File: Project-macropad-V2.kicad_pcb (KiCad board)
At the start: 2 copper layers, 50 parts, among them J1 Conn_01x04_Male, SW1 RotaryEncoder_Switch, SW2 SW_Push, SW3 SW_SPDT

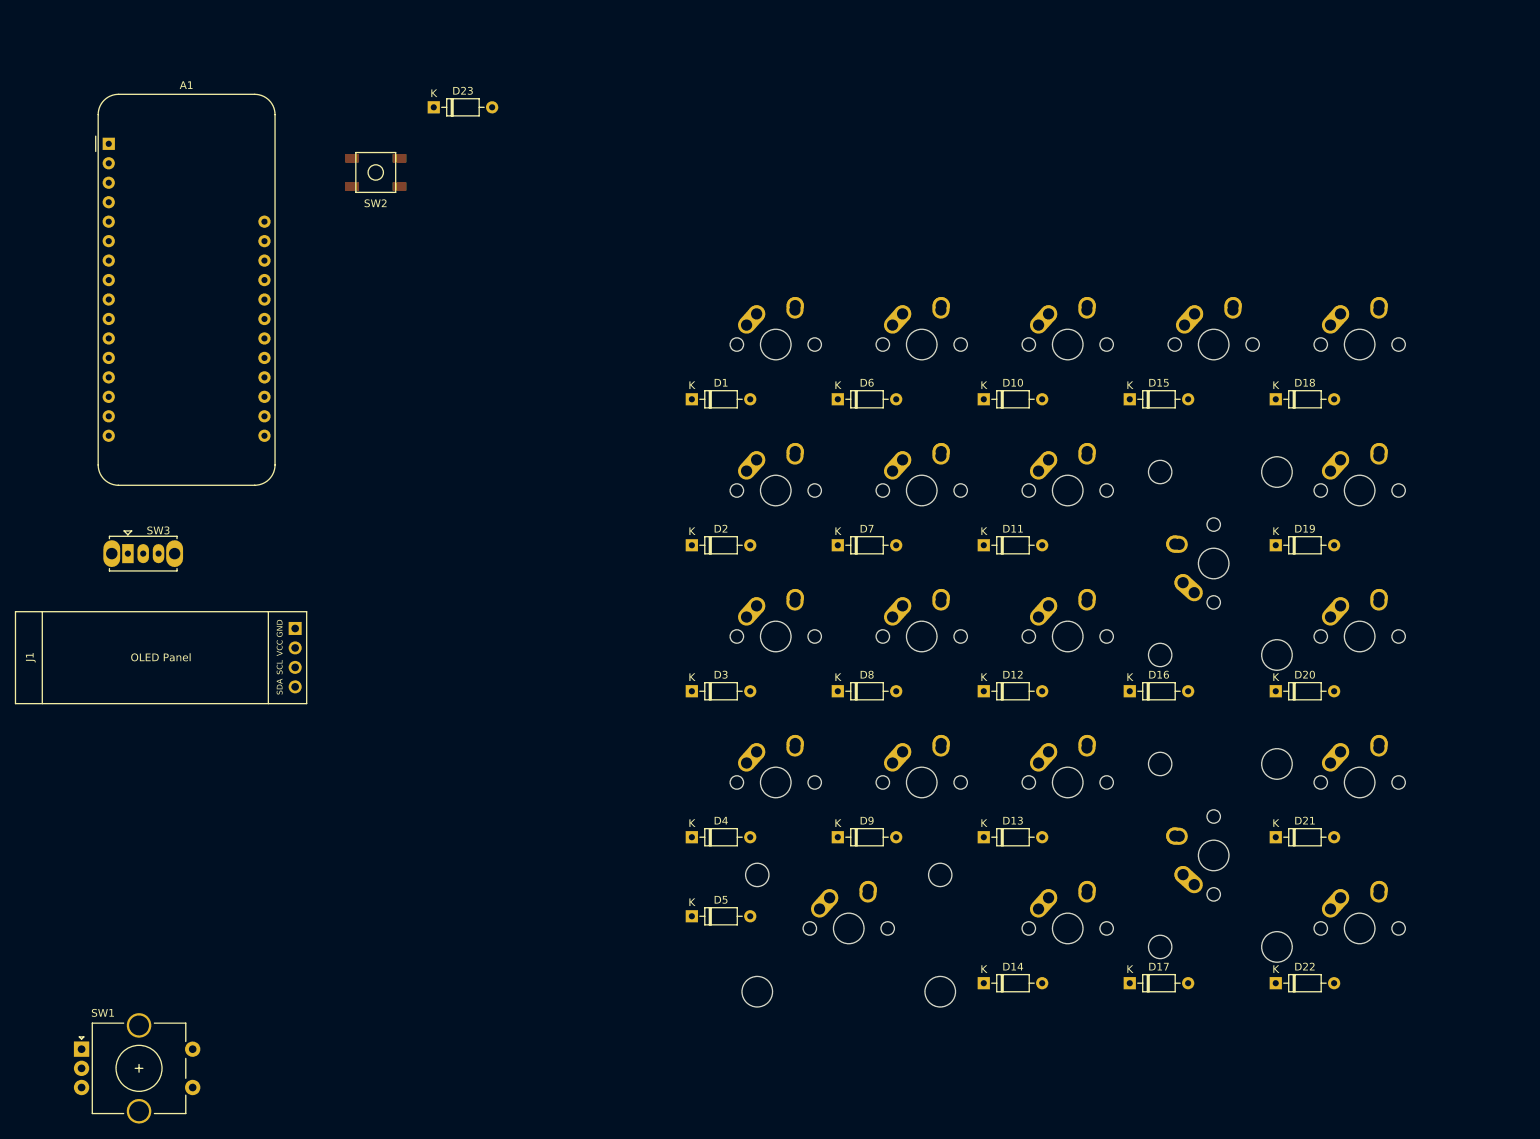
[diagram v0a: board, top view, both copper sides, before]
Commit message: PCB Routing done
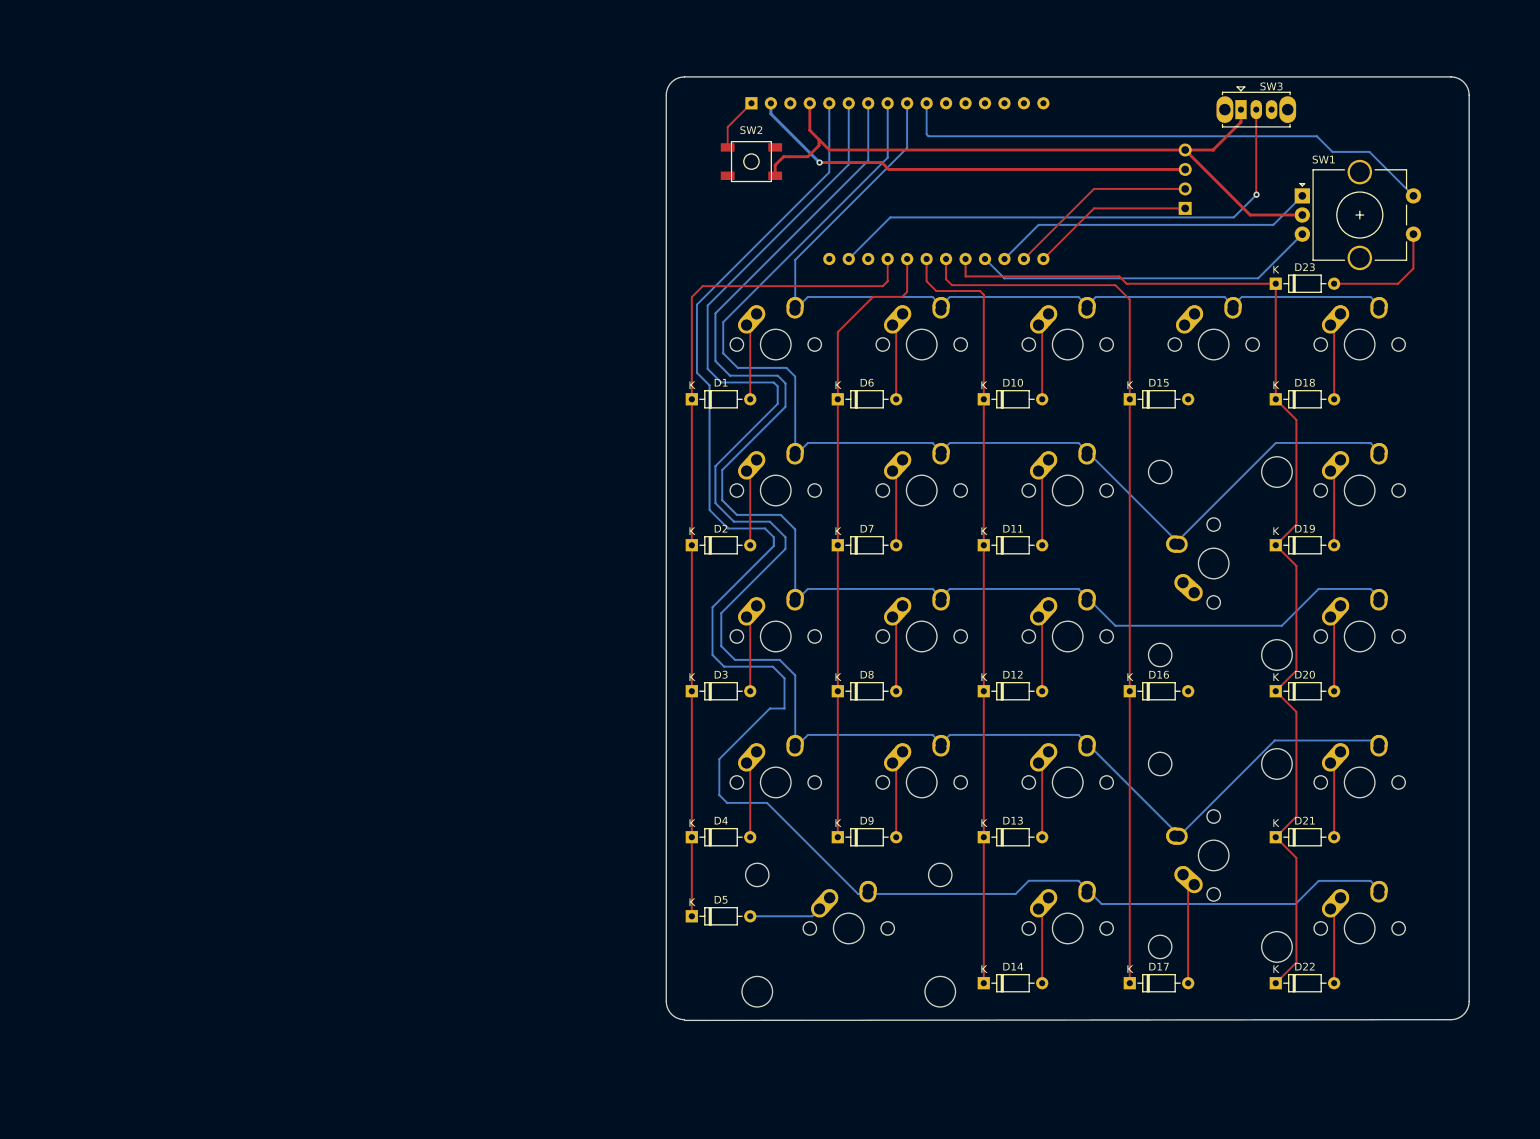
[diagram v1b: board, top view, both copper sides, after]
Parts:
- A1, J1: moved to B.Cu
- moved SW1 194.4 mm to (189.4, 37.7)
- moved SW3 156.4 mm to (181.4, 26.5)
- moved J1 126.6 mm to (137.6, 41.6)
- moved D23 112.3 mm to (185.9, 49.2)
- moved A1 84.0 mm to (117.5, 25.7), turned to -90 degrees
- moved SW2 49.0 mm to (117.5, 33.3), turned to 180 degrees
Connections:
- A1 pad 10: ROT2 -> ROW0
- A1 pad 19: ROW0 -> ROT1
- A1 pad 20: ROW1 -> ROT2
- A1 pad 21: ROW2 -> COL4
- A1 pad 22: ROW3 -> COL3
- A1 pad 23: ROW4 -> COL2
- A1 pad 24: ROW5 -> COL1
- A1 pad 25: ROT1 -> COL0
- A1 pad 5: COL0 -> ROW5
- A1 pad 6: COL1 -> ROW4
- A1 pad 7: COL2 -> ROW3
- A1 pad 8: COL3 -> ROW2
- A1 pad 9: COL4 -> ROW1
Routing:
- net ROW5: track 0.00 -> 215.1 mm
- net ROW4: track 0.00 -> 208.8 mm
- net ROW3: track 0.00 -> 173.8 mm
- net ROW2: track 0.00 -> 151.6 mm
- net COL4: track 0.00 -> 143.4 mm
- net COL3: track 0.00 -> 116.9 mm
- net ROW1: track 0.00 -> 112.7 mm
- net COL0: track 0.00 -> 110.1 mm
- net COL2: track 0.00 -> 100.9 mm
- net GND: track 0.00 -> 92.6 mm
- net COL1: track 0.00 -> 81.4 mm
- net ROW0: track 0.00 -> 70.9 mm
- net Net-(A1-Pad27): track 0.00 -> 67.8 mm, vias 0 -> 1
- net +3V3: track 0.00 -> 58.5 mm, vias 0 -> 1
- net ROT2: track 0.00 -> 44.8 mm
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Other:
- board outline added: 104.8 x 123.1 mm

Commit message: Finished PCB
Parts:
- added G***: LOGO, Dick:Dick_small, F.Cu at (205.6, 29.4)
- D1, D10, D11, D12, D13, D14, D15, D16, D17, D18, D19, D2, D20, D21, D22, D23, D3, D4, D5, D6, D7, D8, D9: moved to B.Cu
- J1: moved to F.Cu
- moved J1 12.2 mm to (137.6, 29.4)
- moved D20 5.32 mm to (190.7, 104.8)
- moved D21 5.32 mm to (190.7, 123.8)
- moved D19 5.32 mm to (190.7, 85.7)
- moved D13 3.37 mm to (150.2, 123.8)
- moved D18 3.37 mm to (188.3, 66.7)
- moved D12 2.38 mm to (147.8, 104.8)
- moved D16 2.38 mm to (166.8, 104.8)
- moved D3 2.38 mm to (109.7, 104.8)
- moved D8 2.38 mm to (128.7, 104.8)
- moved D9 2.38 mm to (128.7, 123.8)
- moved D1 2.38 mm to (109.7, 66.7)
- moved D10 2.38 mm to (147.8, 66.7)
- moved D11 2.38 mm to (147.8, 85.7)
- moved D14 2.38 mm to (147.8, 142.9)
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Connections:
- J1 pad 1: SDA -> GND
- J1 pad 2: SCL -> +3V3
- J1 pad 3: +3V3 -> SCL
- J1 pad 4: GND -> SDA
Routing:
- net Net-(D16-Pad2): track 0.00 -> 15.6 mm
- net Net-(D15-Pad2): track 0.00 -> 12.3 mm
- net Net-(D5-Pad2): track 9.44 -> 20.2 mm
- net Net-(D21-Pad2): track 9.88 -> 15.6 mm
- net Net-(D20-Pad2): track 9.88 -> 15.6 mm
- net Net-(D19-Pad2): track 9.88 -> 15.6 mm
- net COL2: track 100.9 -> 105.3 mm
- net COL4: track 143.4 -> 147.7 mm
- net Net-(D13-Pad2): track 9.88 -> 13.2 mm
- net Net-(D18-Pad2): track 9.88 -> 13.2 mm
- net Net-(D9-Pad2): track 9.88 -> 12.3 mm
- net Net-(D8-Pad2): track 9.88 -> 12.3 mm
- net Net-(D3-Pad2): track 9.88 -> 12.3 mm
- net Net-(D12-Pad2): track 9.88 -> 12.3 mm
- net COL1: track 81.4 -> 83.8 mm
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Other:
- board size 104.8 x 123.1 mm -> 104.8 x 123 mm
- board text added: "Dr.Kreijger"

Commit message: Plate almost done
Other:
- board size 104.8 x 123 mm -> 110.5 x 128.4 mm

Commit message: Plate done
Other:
- board size 110.5 x 128.4 mm -> 119.1 x 138.9 mm
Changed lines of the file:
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@@
   (gr_line (start 113.635 50.673) (end 113.635 63.673) (layer "Edge.Cuts") (width 0.2))
   (gr_line (start 203.835 88.773) (end 203.835 101.773) (layer "Edge.Cuts") (width 0.2))
-  (gr_line (start 106.26725 147.898) (end 211.219002 147.898) (layer "Edge.Cuts") (width 0.2))
-  (gr_circle (center 105.918 21.082) (end 107.518 21.082) (layer "Edge.Cuts") (width 0.2) (fill none))
+  (gr_circle (center 104.775 19.84375) (end 106.375 19.84375) (layer "Edge.Cuts") (width 0.2) (fill none))
   (gr_arc (start 189.835 126.873) (mid 189.981447 126.519447) (end 190.335 126.373) (layer "Edge.Cuts") (width 0.2))
   (gr_arc (start 152.235 83.223) (mid 151.881447 83.076553) (end 151.735 82.723) (layer "Edge.Cuts") (width 0.2))
@@
   (gr_arc (start 127.135 88.273) (mid 127.488553 88.419447) (end 127.635 88.773) (layer "Edge.Cuts") (width 0.2))
   (gr_line (start 132.685 69.723) (end 132.685 82.723) (layer "Edge.Cuts") (width 0.2))
+  (gr_arc (start 211.93125 14.2875) (mid 216.421378 16.147372) (end 218.28125 20.6375) (layer "Edge.Cuts") (width 0.2))
   (gr_line (start 132.685 50.673) (end 132.685 63.673) (layer "Edge.Cuts") (width 0.2))
   (gr_line (start 132.685 107.823) (end 132.685 120.823) (layer "Edge.Cuts") (width 0.2))
   (gr_arc (start 170.785 79.248) (mid 170.931447 78.894447) (end 171.285 78.748) (layer "Edge.Cuts") (width 0.2))
+  (gr_line (start 99.21875 20.6375) (end 99.21875 146.84375) (layer "Edge.Cuts") (width 0.2))
   (gr_arc (start 113.635 107.823) (mid 113.781447 107.469447) (end 114.135 107.323) (layer "Edge.Cuts") (width 0.2))
   (gr_line (start 113.6396 29.448) (end 113.6396 37.084) (layer "Edge.Cuts") (width 0.2))
@@
   (gr_arc (start 127.635 63.673) (mid 127.488553 64.026553) (end 127.135 64.173) (layer "Edge.Cuts") (width 0.2))
   (gr_arc (start 123.16 126.873) (mid 123.306447 126.519447) (end 123.66 126.373) (layer "Edge.Cuts") (width 0.2))
-  (gr_circle (center 212.7506 21.082) (end 214.3506 21.082) (layer "Edge.Cuts") (width 0.2) (fill none))
+  (gr_circle (center 212.725 19.84375) (end 214.325 19.84375) (layer "Edge.Cuts") (width 0.2) (fill none))
   (gr_line (start 152.235 121.323) (end 165.235 121.323) (layer "Edge.Cuts") (width 0.2))
   (gr_arc (start 203.335 50.173) (mid 203.688553 50.319447) (end 203.835 50.673) (layer "Edge.Cuts") (width 0.2))
@@
   (gr_arc (start 127.135 50.173) (mid 127.488553 50.319447) (end 127.635 50.673) (layer "Edge.Cuts") (width 0.2))
   (gr_line (start 114.135 107.323) (end 127.135 107.323) (layer "Edge.Cuts") (width 0.2))
-  (gr_line (start 213.600252 145.51675) (end 213.600252 22.09165) (layer "Edge.Cuts") (width 0.2))
-  (gr_arc (start 213.600252 145.51675) (mid 212.9028 147.200548) (end 211.219002 147.898) (layer "Edge.Cuts") (width 0.2))
   (gr_line (start 170.785 79.248) (end 170.785 92.248) (layer "Edge.Cuts") (width 0.2))
   (gr_arc (start 189.835 50.673) (mid 189.981447 50.319447) (end 190.335 50.173) (layer "Edge.Cuts") (width 0.2))
@@
   (gr_line (start 170.785 50.673) (end 170.785 63.673) (layer "Edge.Cuts") (width 0.2))
   (gr_arc (start 183.285 108.41) (mid 183.638553 108.556447) (end 183.785 108.91) (layer "Edge.Cuts") (width 0.2))
-  (gr_line (start 211.219002 19.7104) (end 106.26725 19.7104) (layer "Edge.Cuts") (width 0.2))
   (gr_line (start 190.335 88.273) (end 203.335 88.273) (layer "Edge.Cuts") (width 0.2))
   (gr_line (start 151.735 50.673) (end 151.735 63.673) (layer "Edge.Cuts") (width 0.2))
@@
   (gr_arc (start 168.785 70.81) (mid 168.931447 70.456447) (end 169.285 70.31) (layer "Edge.Cuts") (width 0.2))
   (gr_arc (start 203.835 101.773) (mid 203.688553 102.126553) (end 203.335 102.273) (layer "Edge.Cuts") (width 0.2))
+  (gr_line (start 218.28125 146.84375) (end 218.28125 20.6375) (layer "Edge.Cuts") (width 0.2))
   (gr_line (start 190.335 50.173) (end 203.335 50.173) (layer "Edge.Cuts") (width 0.2))
   (gr_arc (start 165.235 88.273) (mid 165.588553 88.419447) (end 165.735 88.773) (layer "Edge.Cuts") (width 0.2))
@@
   (gr_line (start 208.75625 22.225) (end 108.74375 22.225) (layer "Edge.Cuts") (width 0.1))
   (gr_line (start 146.685 88.773) (end 146.685 101.773) (layer "Edge.Cuts") (width 0.2))
+  (gr_arc (start 105.56875 153.19375) (mid 101.078622 151.333878) (end 99.21875 146.84375) (layer "Edge.Cuts") (width 0.2))
   (gr_arc (start 203.335 69.223) (mid 203.688553 69.369447) (end 203.835 69.723) (layer "Edge.Cuts") (width 0.2))
   (gr_arc (start 208.75625 22.225) (mid 210.440048 22.922452) (end 211.1375 24.60625) (layer "Edge.Cuts") (width 0.1))
@@
   (gr_line (start 113.635 69.723) (end 113.635 82.723) (layer "Edge.Cuts") (width 0.2))
   (gr_arc (start 189.835 88.773) (mid 189.981447 88.419447) (end 190.335 88.273) (layer "Edge.Cuts") (width 0.2))
-  (gr_arc (start 211.219002 19.7104) (mid 212.9028 20.407852) (end 213.600252 22.09165) (layer "Edge.Cuts") (width 0.2))
   (gr_line (start 189.835 69.723) (end 189.835 82.723) (layer "Edge.Cuts") (width 0.2))
   (gr_arc (start 211.1375 142.875) (mid 210.440048 144.558798) (end 208.75625 145.25625) (layer "Edge.Cuts") (width 0.1))
   (gr_line (start 183.285 115.41) (end 169.285 115.41) (layer "Edge.Cuts") (width 0.2))
+  (gr_line (start 211.93125 14.2875) (end 105.56875 14.2875) (layer "Edge.Cuts") (width 0.2))
   (gr_line (start 114.135 50.173) (end 127.135 50.173) (layer "Edge.Cuts") (width 0.2))
+  (gr_arc (start 218.28125 146.84375) (mid 216.421378 151.333878) (end 211.93125 153.19375) (layer "Edge.Cuts") (width 0.2))
   (gr_line (start 152.235 64.173) (end 165.235 64.173) (layer "Edge.Cuts") (width 0.2))
   (gr_line (start 114.135 88.273) (end 127.135 88.273) (layer "Edge.Cuts") (width 0.2))
@@
   (gr_arc (start 113.635 69.723) (mid 113.781447 69.369447) (end 114.135 69.223) (layer "Edge.Cuts") (width 0.2))
   (gr_arc (start 146.685 63.673) (mid 146.538553 64.026553) (end 146.185 64.173) (layer "Edge.Cuts") (width 0.2))
-  (gr_line (start 103.886 145.51675) (end 103.886 22.09165) (layer "Edge.Cuts") (width 0.2))
   (gr_arc (start 190.335 140.373) (mid 189.981447 140.226553) (end 189.835 139.873) (layer "Edge.Cuts") (width 0.2))
   (gr_line (start 123.66 140.373) (end 136.66 140.373) (layer "Edge.Cuts") (width 0.2))
-  (gr_arc (start 103.886 22.09165) (mid 104.583452 20.407852) (end 106.26725 19.7104) (layer "Edge.Cuts") (width 0.2))
   (gr_arc (start 146.685 101.773) (mid 146.538553 102.126553) (end 146.185 102.273) (layer "Edge.Cuts") (width 0.2))
   (gr_arc (start 113.635 88.773) (mid 113.781447 88.419447) (end 114.135 88.273) (layer "Edge.Cuts") (width 0.2))
@@
   (gr_line (start 127.635 107.823) (end 127.635 120.823) (layer "Edge.Cuts") (width 0.2))
   (gr_line (start 168.785 94.686) (end 168.785 100.686) (layer "Edge.Cuts") (width 0.2))
-  (gr_circle (center 105.918 146.1262) (end 107.518 146.1262) (layer "Edge.Cuts") (width 0.2) (fill none))
+  (gr_circle (center 104.775 147.6375) (end 106.375 147.6375) (layer "Edge.Cuts") (width 0.2) (fill none))
   (gr_line (start 108.74375 145.25625) (end 208.75625 145.25625) (layer "Edge.Cuts") (width 0.1))
   (gr_arc (start 183.285 70.31) (mid 183.638553 70.456447) (end 183.785 70.81) (layer "Edge.Cuts") (width 0.2))
@@
   (gr_line (start 152.235 102.273) (end 165.235 102.273) (layer "Edge.Cuts") (width 0.2))
   (gr_line (start 168.785 70.81) (end 168.785 76.81) (layer "Edge.Cuts") (width 0.2))
+  (gr_line (start 105.56875 153.19375) (end 211.93125 153.19375) (layer "Edge.Cuts") (width 0.2))
   (gr_line (start 168.785 108.91) (end 168.785 114.91) (layer "Edge.Cuts") (width 0.2))
   (gr_line (start 113.635 88.773) (end 113.635 101.773) (layer "Edge.Cuts") (width 0.2))
@@
   (gr_arc (start 127.635 101.773) (mid 127.488553 102.126553) (end 127.135 102.273) (layer "Edge.Cuts") (width 0.2))
   (gr_arc (start 132.685 88.773) (mid 132.831447 88.419447) (end 133.185 88.273) (layer "Edge.Cuts") (width 0.2))
+  (gr_arc (start 99.21875 20.6375) (mid 101.078622 16.147372) (end 105.56875 14.2875) (layer "Edge.Cuts") (width 0.2))
   (gr_arc (start 190.335 83.223) (mid 189.981447 83.076553) (end 189.835 82.723) (layer "Edge.Cuts") (width 0.2))
   (gr_line (start 121.3104 37.1) (end 113.6396 37.1) (layer "Edge.Cuts") (width 0.2))
@@
   (gr_line (start 127.635 88.773) (end 127.635 101.773) (layer "Edge.Cuts") (width 0.2))
   (gr_line (start 152.235 50.173) (end 165.235 50.173) (layer "Edge.Cuts") (width 0.2))
-  (gr_arc (start 106.26725 147.898) (mid 104.583452 147.200548) (end 103.886 145.51675) (layer "Edge.Cuts") (width 0.2))
   (gr_arc (start 145.598 141.873) (mid 145.451553 142.226553) (end 145.098 142.373) (layer "Edge.Cuts") (width 0.2))
   (gr_arc (start 189.835 107.823) (mid 189.981447 107.469447) (end 190.335 107.323) (layer "Edge.Cuts") (width 0.2))
@@
   (gr_line (start 190.335 126.373) (end 203.335 126.373) (layer "Edge.Cuts") (width 0.2))
   (gr_arc (start 114.135 83.223) (mid 113.781447 83.076553) (end 113.635 82.723) (layer "Edge.Cuts") (width 0.2))
-  (gr_circle (center 212.7506 146.2532) (end 214.3506 146.2532) (layer "Edge.Cuts") (width 0.2) (fill none))
+  (gr_circle (center 212.725 147.6375) (end 214.325 147.6375) (layer "Edge.Cuts") (width 0.2) (fill none))
   (gr_arc (start 165.735 82.723) (mid 165.588553 83.076553) (end 165.235 83.223) (layer "Edge.Cuts") (width 0.2))
   (gr_line (start 133.185 69.223) (end 146.185 69.223) (layer "Edge.Cuts") (width 0.2))
